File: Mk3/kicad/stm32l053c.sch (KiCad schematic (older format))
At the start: 42 parts, among them J1 GND, J2 GND, J3 TX, J4 GND, J5 TEST_1P, J6 TEST_1P, J7 TEST_1P, J8 RX, P1 SWD, U1 AP2112, U2 STM32L053C8_LQFP48, U3 ADS1015, U4 UFL_SMA, U5 RFM92/95

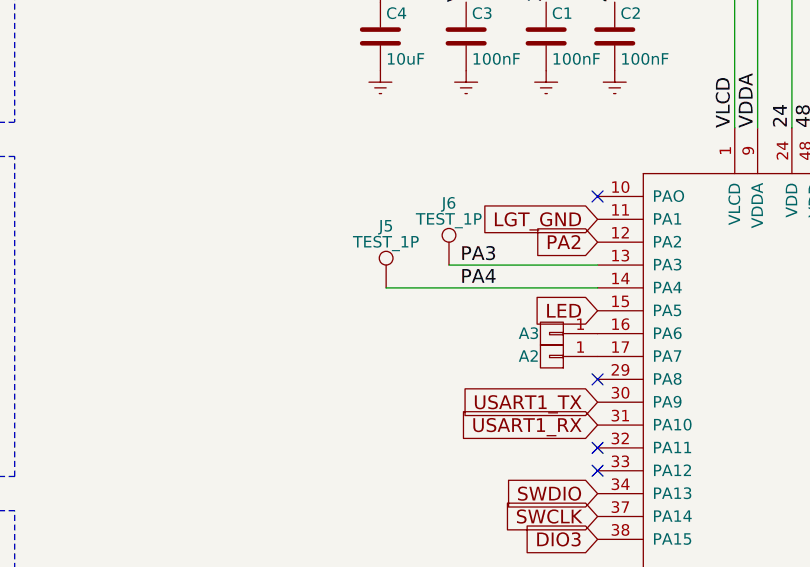
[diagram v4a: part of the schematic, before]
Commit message: Pull up resistor for the DS18B20 one wire temperature sensor
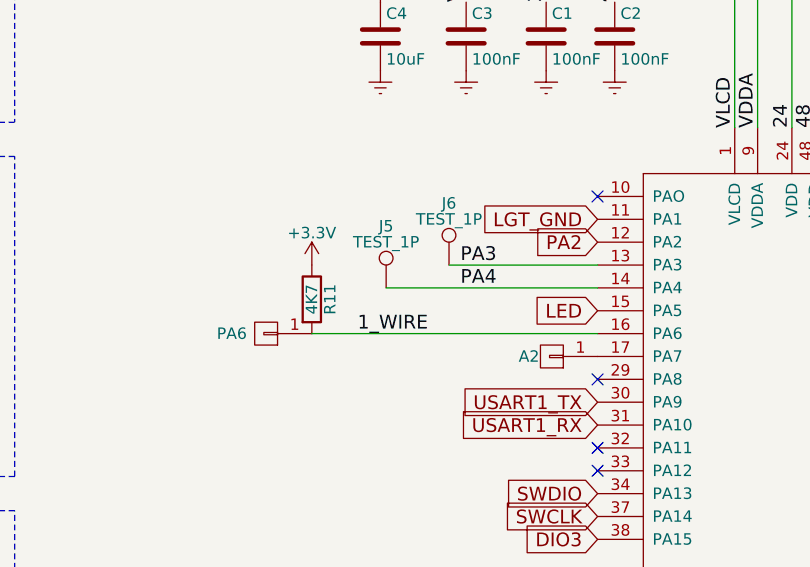
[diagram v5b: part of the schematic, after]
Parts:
- added R11: 4K7, Resistors_SMD:R_0805_HandSoldering, symbol R
- renumbered A3 to PA6
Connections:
- net +3V3: now also R11.1
- net 1_WIRE: now reaches PA6.1 (P1), U2.16 (PA6)
- net 1_WIRE: now also R11.2
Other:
- moved on the sheet: PA6
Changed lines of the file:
@@
 $EndDescr
 $Comp
-L Earth #PWR8
+L Earth #PWR29
 U 1 1 58021BE1
 P 7400 1900
-F 0 "#PWR8" H 7400 1650 50  0001 C CNN
+F 0 "#PWR29" H 7400 1650 50  0001 C CNN
 F 1 "Earth" H 7400 1750 50  0001 C CNN
 F 2 "" H 7400 1900 50  0000 C CNN
@@
 $EndComp
 $Comp
-L GNDA #PWR25
+L GNDA #PWR34
 U 1 1 58021F75
 P 9325 5925
-F 0 "#PWR25" H 9325 5675 50  0001 C CNN
+F 0 "#PWR34" H 9325 5675 50  0001 C CNN
 F 1 "GNDA" H 9325 5775 50  0000 C CNN
 F 2 "" H 9325 5925 50  0000 C CNN
@@
 $EndComp
 $Comp
-L Earth #PWR26
+L Earth #PWR35
 U 1 1 58021F89
 P 9825 5925
-F 0 "#PWR26" H 9825 5675 50  0001 C CNN
+F 0 "#PWR35" H 9825 5675 50  0001 C CNN
 F 1 "Earth" H 9825 5775 50  0001 C CNN
 F 2 "" H 9825 5925 50  0000 C CNN
@@
 $EndComp
 $Comp
-L GNDA #PWR27
+L GNDA #PWR31
 U 1 1 58022154
 P 8175 5950
-F 0 "#PWR27" H 8175 5700 50  0001 C CNN
+F 0 "#PWR31" H 8175 5700 50  0001 C CNN
 F 1 "GNDA" H 8175 5800 50  0000 C CNN
 F 2 "" H 8175 5950 50  0000 C CNN
@@
 $EndComp
 $Comp
-L Earth #PWR28
+L Earth #PWR33
 U 1 1 580221FA
 P 8675 5950
-F 0 "#PWR28" H 8675 5700 50  0001 C CNN
+F 0 "#PWR33" H 8675 5700 50  0001 C CNN
 F 1 "Earth" H 8675 5800 50  0001 C CNN
 F 2 "" H 8675 5950 50  0000 C CNN
@@
 $EndComp
 $Comp
-L Earth #PWR13
+L Earth #PWR7
 U 1 1 580369A9
 P 2425 3075
-F 0 "#PWR13" H 2425 2825 50  0001 C CNN
+F 0 "#PWR7" H 2425 2825 50  0001 C CNN
 F 1 "Earth" H 2425 2925 50  0001 C CNN
 F 2 "" H 2425 3075 50  0000 C CNN
@@
 NRST
 $Comp
-L Earth #PWR6
+L Earth #PWR26
 U 1 1 58039244
 P 6675 1900
-F 0 "#PWR6" H 6675 1650 50  0001 C CNN
+F 0 "#PWR26" H 6675 1650 50  0001 C CNN
 F 1 "Earth" H 6675 1750 50  0001 C CNN
 F 2 "" H 6675 1900 50  0000 C CNN
@@
 $EndComp
 $Comp
-L Earth #PWR7
+L Earth #PWR27
 U 1 1 5803BDC8
 P 7050 1900
-F 0 "#PWR7" H 7050 1650 50  0001 C CNN
+F 0 "#PWR27" H 7050 1650 50  0001 C CNN
 F 1 "Earth" H 7050 1750 50  0001 C CNN
 F 2 "" H 7050 1900 50  0000 C CNN
@@
 $EndComp
 $Comp
-L Earth #PWR21
+L Earth #PWR28
 U 1 1 58065816
 P 7275 4950
-F 0 "#PWR21" H 7275 4700 50  0001 C CNN
+F 0 "#PWR28" H 7275 4700 50  0001 C CNN
 F 1 "Earth" H 7275 4800 50  0001 C CNN
 F 2 "" H 7275 4950 50  0000 C CNN
@@
 $EndComp
 $Comp
-L Earth #PWR11
+L Earth #PWR15
 U 1 1 58077163
 P 3550 2800
-F 0 "#PWR11" H 3550 2550 50  0001 C CNN
+F 0 "#PWR15" H 3550 2550 50  0001 C CNN
 F 1 "Earth" H 3550 2650 50  0001 C CNN
 F 2 "" H 3550 2800 50  0000 C CNN
@@
 Place on Top layer
 $Comp
-L Earth #PWR23
+L Earth #PWR11
 U 1 1 592DF55A
 P 2900 5450
-F 0 "#PWR23" H 2900 5200 50  0001 C CNN
+F 0 "#PWR11" H 2900 5200 50  0001 C CNN
 F 1 "Earth" H 2900 5300 50  0001 C CNN
 F 2 "" H 2900 5450 50  0000 C CNN
@@
 NoConn ~ 4150 1625
 $Comp
-L Earth #PWR10
+L Earth #PWR17
 U 1 1 592F1C89
 P 3750 1925
-F 0 "#PWR10" H 3750 1675 50  0001 C CNN
+F 0 "#PWR17" H 3750 1675 50  0001 C CNN
 F 1 "Earth" H 3750 1775 50  0001 C CNN
 F 2 "" H 3750 1925 50  0000 C CNN
@@
 RFM_RST
 $Comp
-L +3.3V #PWR1
+L +3.3V #PWR21
 U 1 1 592F43A5
 P 4450 1175
-F 0 "#PWR1" H 4450 1025 50  0001 C CNN
+F 0 "#PWR21" H 4450 1025 50  0001 C CNN
 F 1 "+3.3V" H 4450 1315 50  0000 C CNN
 F 2 "" H 4450 1175 50  0001 C CNN
@@
 $EndComp
 $Comp
-L +3.3V #PWR12
+L +3.3V #PWR5
 U 1 1 592F4BC3
 P 1925 2875
-F 0 "#PWR12" H 1925 2725 50  0001 C CNN
+F 0 "#PWR5" H 1925 2725 50  0001 C CNN
 F 1 "+3.3V" H 1925 3015 50  0000 C CNN
 F 2 "" H 1925 2875 50  0001 C CNN
@@
 $EndComp
 $Comp
-L +3.3V #PWR2
+L +3.3V #PWR32
 U 1 1 592F4E66
 P 8475 1425
-F 0 "#PWR2" H 8475 1275 50  0001 C CNN
+F 0 "#PWR32" H 8475 1275 50  0001 C CNN
 F 1 "+3.3V" H 8475 1565 50  0000 C CNN
 F 2 "" H 8475 1425 50  0001 C CNN
@@
 $EndComp
 $Comp
-L +3.3V #PWR32
+L +3.3V #PWR22
 U 1 1 592F53D7
 P 4775 6725
-F 0 "#PWR32" H 4775 6575 50  0001 C CNN
+F 0 "#PWR22" H 4775 6575 50  0001 C CNN
 F 1 "+3.3V" H 4775 6865 50  0000 C CNN
 F 2 "" H 4775 6725 50  0001 C CNN
@@
 $EndComp
 $Comp
-L +3.3V #PWR3
+L +3.3V #PWR25
 U 1 1 592F54CD
 P 6675 1600
-F 0 "#PWR3" H 6675 1450 50  0001 C CNN
+F 0 "#PWR25" H 6675 1450 50  0001 C CNN
 F 1 "+3.3V" H 6675 1740 50  0000 C CNN
 F 2 "" H 6675 1600 50  0001 C CNN
@@
 NoConn ~ 7625 3550
 $Comp
-L Earth #PWR33
+L Earth #PWR23
 U 1 1 592F7C8A
 P 4775 7025
-F 0 "#PWR33" H 4775 6775 50  0001 C CNN
+F 0 "#PWR23" H 4775 6775 50  0001 C CNN
 F 1 "Earth" H 4775 6875 50  0001 C CNN
 F 2 "" H 4775 7025 50  0000 C CNN
@@
 $EndComp
 $Comp
-L Earth #PWR29
+L Earth #PWR9
 U 1 1 592F7CF0
 P 2750 6425
-F 0 "#PWR29" H 2750 6175 50  0001 C CNN
+F 0 "#PWR9" H 2750 6175 50  0001 C CNN
 F 1 "Earth" H 2750 6275 50  0001 C CNN
 F 2 "" H 2750 6425 50  0000 C CNN
@@
 $EndComp
 $Comp
-L Earth #PWR34
+L Earth #PWR12
 U 1 1 592F7EE4
 P 3225 7125
-F 0 "#PWR34" H 3225 6875 50  0001 C CNN
+F 0 "#PWR12" H 3225 6875 50  0001 C CNN
 F 1 "Earth" H 3225 6975 50  0001 C CNN
 F 2 "" H 3225 7125 50  0000 C CNN
@@
 $EndComp
 $Comp
-L Earth #PWR30
+L Earth #PWR2
 U 1 1 592F80DC
 P 1300 6575
-F 0 "#PWR30" H 1300 6325 50  0001 C CNN
+F 0 "#PWR2" H 1300 6325 50  0001 C CNN
 F 1 "Earth" H 1300 6425 50  0001 C CNN
 F 2 "" H 1300 6575 50  0000 C CNN
@@
 $EndComp
 $Comp
-L Earth #PWR31
+L Earth #PWR6
 U 1 1 592F814F
 P 2050 6600
-F 0 "#PWR31" H 2050 6350 50  0001 C CNN
+F 0 "#PWR6" H 2050 6350 50  0001 C CNN
 F 1 "Earth" H 2050 6450 50  0001 C CNN
 F 2 "" H 2050 6600 50  0000 C CNN
@@
 $EndComp
 $Comp
-L Earth #PWR22
+L Earth #PWR18
 U 1 1 59301904
 P 3800 5150
-F 0 "#PWR22" H 3800 4900 50  0001 C CNN
+F 0 "#PWR18" H 3800 4900 50  0001 C CNN
 F 1 "Earth" H 3800 5000 50  0001 C CNN
 F 2 "" H 3800 5150 50  0000 C CNN
@@
 $EndComp
 $Comp
-L Earth #PWR19
+L Earth #PWR16
 U 1 1 593024E3
 P 3700 4450
-F 0 "#PWR19" H 3700 4200 50  0001 C CNN
+F 0 "#PWR16" H 3700 4200 50  0001 C CNN
 F 1 "Earth" H 3700 4300 50  0001 C CNN
 F 2 "" H 3700 4450 50  0000 C CNN
@@
 $EndComp
 $Comp
-L +3.3V #PWR17
+L +3.3V #PWR10
 U 1 1 59303669
 P 2900 4150
-F 0 "#PWR17" H 2900 4000 50  0001 C CNN
+F 0 "#PWR10" H 2900 4000 50  0001 C CNN
 F 1 "+3.3V" H 2900 4290 50  0000 C CNN
 F 2 "" H 2900 4150 50  0001 C CNN
@@
 $EndComp
 $Comp
-L +3.3V #PWR18
+L +3.3V #PWR19
 U 1 1 59303771
 P 4100 4150
-F 0 "#PWR18" H 4100 4000 50  0001 C CNN
+F 0 "#PWR19" H 4100 4000 50  0001 C CNN
 F 1 "+3.3V" H 4100 4290 50  0000 C CNN
 F 2 "" H 4100 4150 50  0001 C CNN
@@
 $EndComp
 $Comp
-L Earth #PWR4
+L Earth #PWR8
 U 1 1 59316863
 P 2600 1675
-F 0 "#PWR4" H 2600 1425 50  0001 C CNN
+F 0 "#PWR8" H 2600 1425 50  0001 C CNN
 F 1 "Earth" H 2600 1525 50  0001 C CNN
 F 2 "" H 2600 1675 50  0000 C CNN
@@
 $EndComp
 $Comp
-L Earth #PWR20
+L Earth #PWR1
 U 1 1 593290F6
 P 1275 4775
-F 0 "#PWR20" H 1275 4525 50  0001 C CNN
+F 0 "#PWR1" H 1275 4525 50  0001 C CNN
 F 1 "Earth" H 1275 4625 50  0001 C CNN
 F 2 "" H 1275 4775 50  0000 C CNN
@@
 $EndComp
 $Comp
-L Earth #PWR5
+L Earth #PWR3
 U 1 1 59355822
 P 1650 1900
-F 0 "#PWR5" H 1650 1650 50  0001 C CNN
+F 0 "#PWR3" H 1650 1650 50  0001 C CNN
 F 1 "Earth" H 1650 1750 50  0001 C CNN
 F 2 "" H 1650 1900 50  0000 C CNN
@@
 $EndComp
 $Comp
-L Earth #PWR24
+L Earth #PWR4
 U 1 1 59357323
 P 1900 5500
-F 0 "#PWR24" H 1900 5250 50  0001 C CNN
+F 0 "#PWR4" H 1900 5250 50  0001 C CNN
 F 1 "Earth" H 1900 5350 50  0001 C CNN
 F 2 "" H 1900 5500 50  0000 C CNN
@@
 $EndComp
 $Comp
-L Earth #PWR9
+L Earth #PWR30
 U 1 1 59375C9C
 P 7700 1900
-F 0 "#PWR9" H 7700 1650 50  0001 C CNN
+F 0 "#PWR30" H 7700 1650 50  0001 C CNN
 F 1 "Earth" H 7700 1750 50  0001 C CNN
 F 2 "" H 7700 1900 50  0000 C CNN
@@
 $EndComp
 $Comp
-L Earth #PWR16
+L Earth #PWR20
 U 1 1 59379ABF
 P 4175 3450
-F 0 "#PWR16" H 4175 3200 50  0001 C CNN
+F 0 "#PWR20" H 4175 3200 50  0001 C CNN
 F 1 "Earth" H 4175 3300 50  0001 C CNN
 F 2 "" H 4175 3450 50  0000 C CNN
@@
 $EndComp
 $Comp
-L CONN_01X01 A3
+L CONN_01X01 PA6
 U 1 1 593959A7
-P 7425 3050
-F 0 "A3" H 7525 3050 50  0000 C CNN
-F 1 "A3" V 7525 3050 50  0001 C CNN
-F 2 "Pin_Headers:Pin_Header_Straight_1x01_Pitch2.54mm" H 7425 3050 50  0001 C CNN
-F 3 "" H 7425 3050 50  0001 C CNN
-	1    7425 3050
+P 6175 3050
+F 0 "PA6" H 6325 3050 50  0000 C CNN
+F 1 "A3" V 6275 3050 50  0001 C CNN
+F 2 "Pin_Headers:Pin_Header_Straight_1x01_Pitch2.54mm" H 6175 3050 50  0001 C CNN
+F 3 "" H 6175 3050 50  0001 C CNN
+	1    6175 3050
 	-1   0    0    1
 $EndComp
@@
 $EndComp
 $Comp
-L Earth #PWR15
+L Earth #PWR14
 U 1 1 593AA95B
 P 3525 3425
-F 0 "#PWR15" H 3525 3175 50  0001 C CNN
+F 0 "#PWR14" H 3525 3175 50  0001 C CNN
 F 1 "Earth" H 3525 3275 50  0001 C CNN
 F 2 "" H 3525 3425 50  0000 C CNN
@@
 $EndComp
 $Comp
-L Earth #PWR14
+L Earth #PWR13
 U 1 1 593AA9D2
 P 3525 3175
-F 0 "#PWR14" H 3525 2925 50  0001 C CNN
+F 0 "#PWR13" H 3525 2925 50  0001 C CNN
 F 1 "Earth" H 3525 3025 50  0001 C CNN
 F 2 "" H 3525 3175 50  0000 C CNN
@@
 Connection ~ 4400 4950
 Connection ~ 4200 4250
+$Comp
+L R R11
+U 1 1 594FB0BF
+P 6375 2900
+F 0 "R11" V 6455 2900 50  0000 C CNN
+F 1 "4K7" V 6375 2900 50  0000 C CNN
+F 2 "Resistors_SMD:R_0805_HandSoldering" V 6305 2900 50  0001 C CNN
+F 3 "" H 6375 2900 50  0000 C CNN
+	1    6375 2900
+	1    0    0    -1
+$EndComp
+$Comp
+L +3.3V #PWR24
+U 1 1 594FB3E7
+P 6375 2750
+F 0 "#PWR24" H 6375 2600 50  0001 C CNN
+F 1 "+3.3V" H 6375 2890 50  0000 C CNN
+F 2 "" H 6375 2750 50  0001 C CNN
+F 3 "" H 6375 2750 50  0001 C CNN
+	1    6375 2750
+	1    0    0    -1
+$EndComp
+Wire Wire Line
+	7625 3050 6375 3050
+Text Label 6575 3050 0    60   ~ 0
+1_WIRE
 $EndSCHEMATC

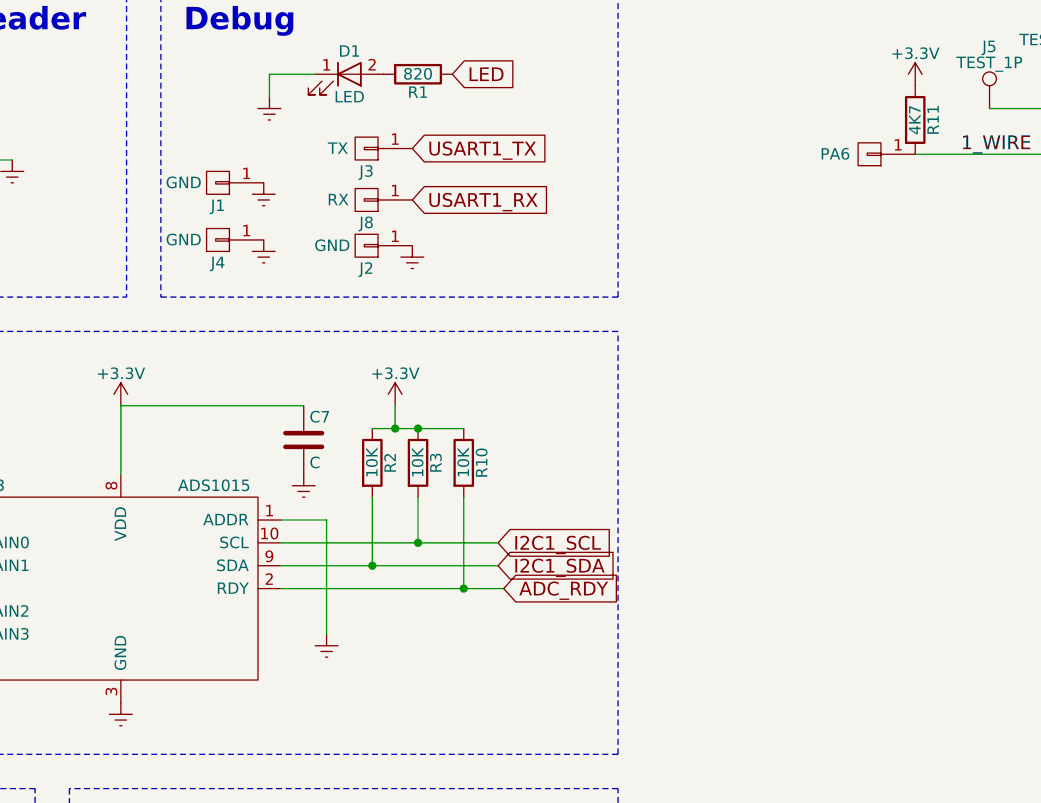
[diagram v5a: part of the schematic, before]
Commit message: Extra 3v3 pins
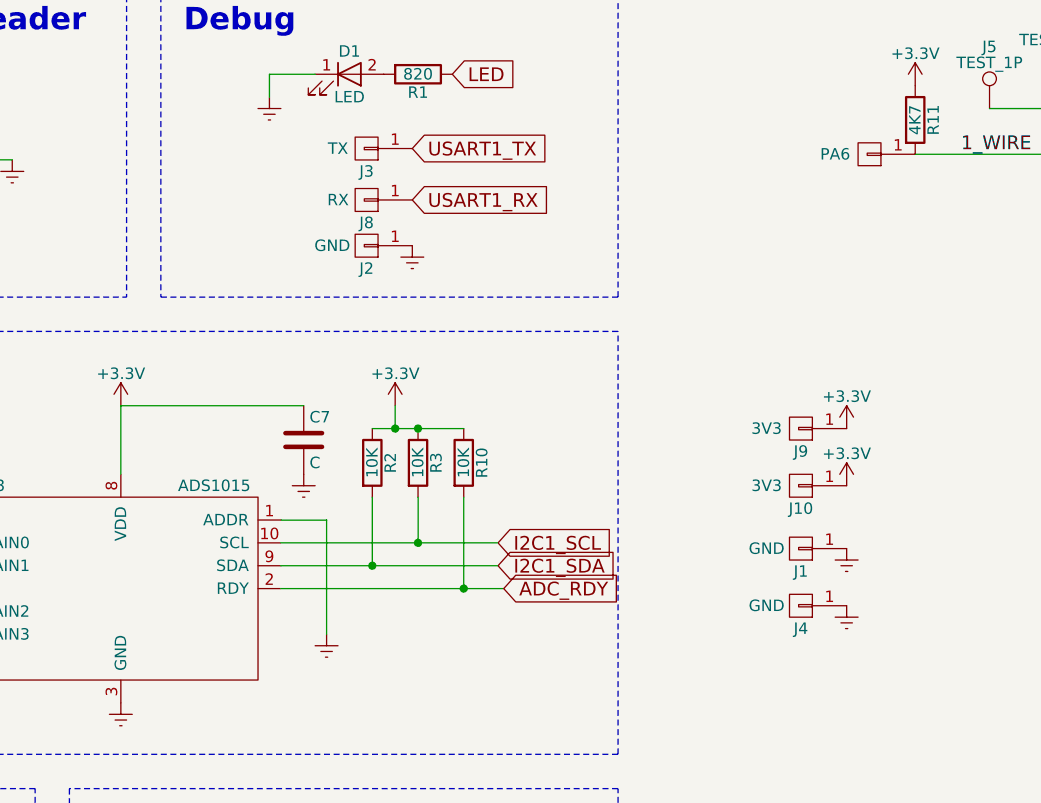
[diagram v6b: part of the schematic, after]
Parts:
- added J10, J9: 3V3, Pin_Headers:Pin_Header_Straight_1x01_Pitch2.54mm, symbol CONN_01X01
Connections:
- net +3V3: now also J10.1 (P1), J9.1 (P1)
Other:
- moved on the sheet: J1, J4

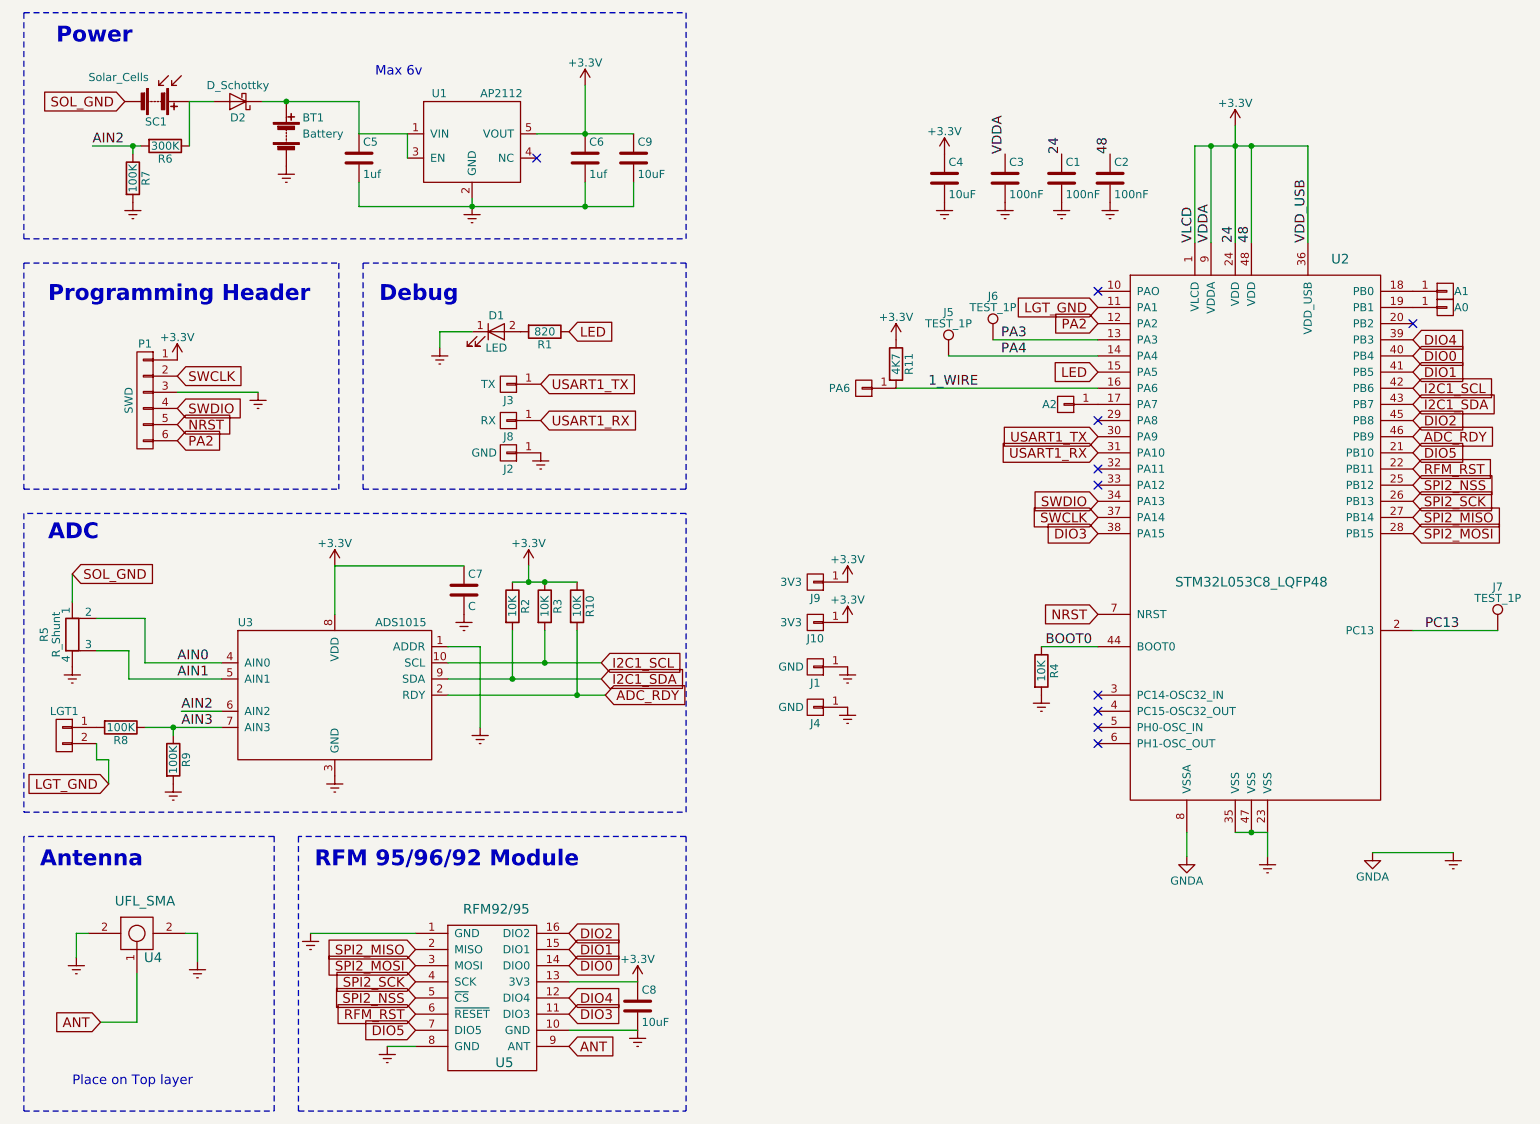
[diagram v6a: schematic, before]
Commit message: Measure battery voltage with the external ADC
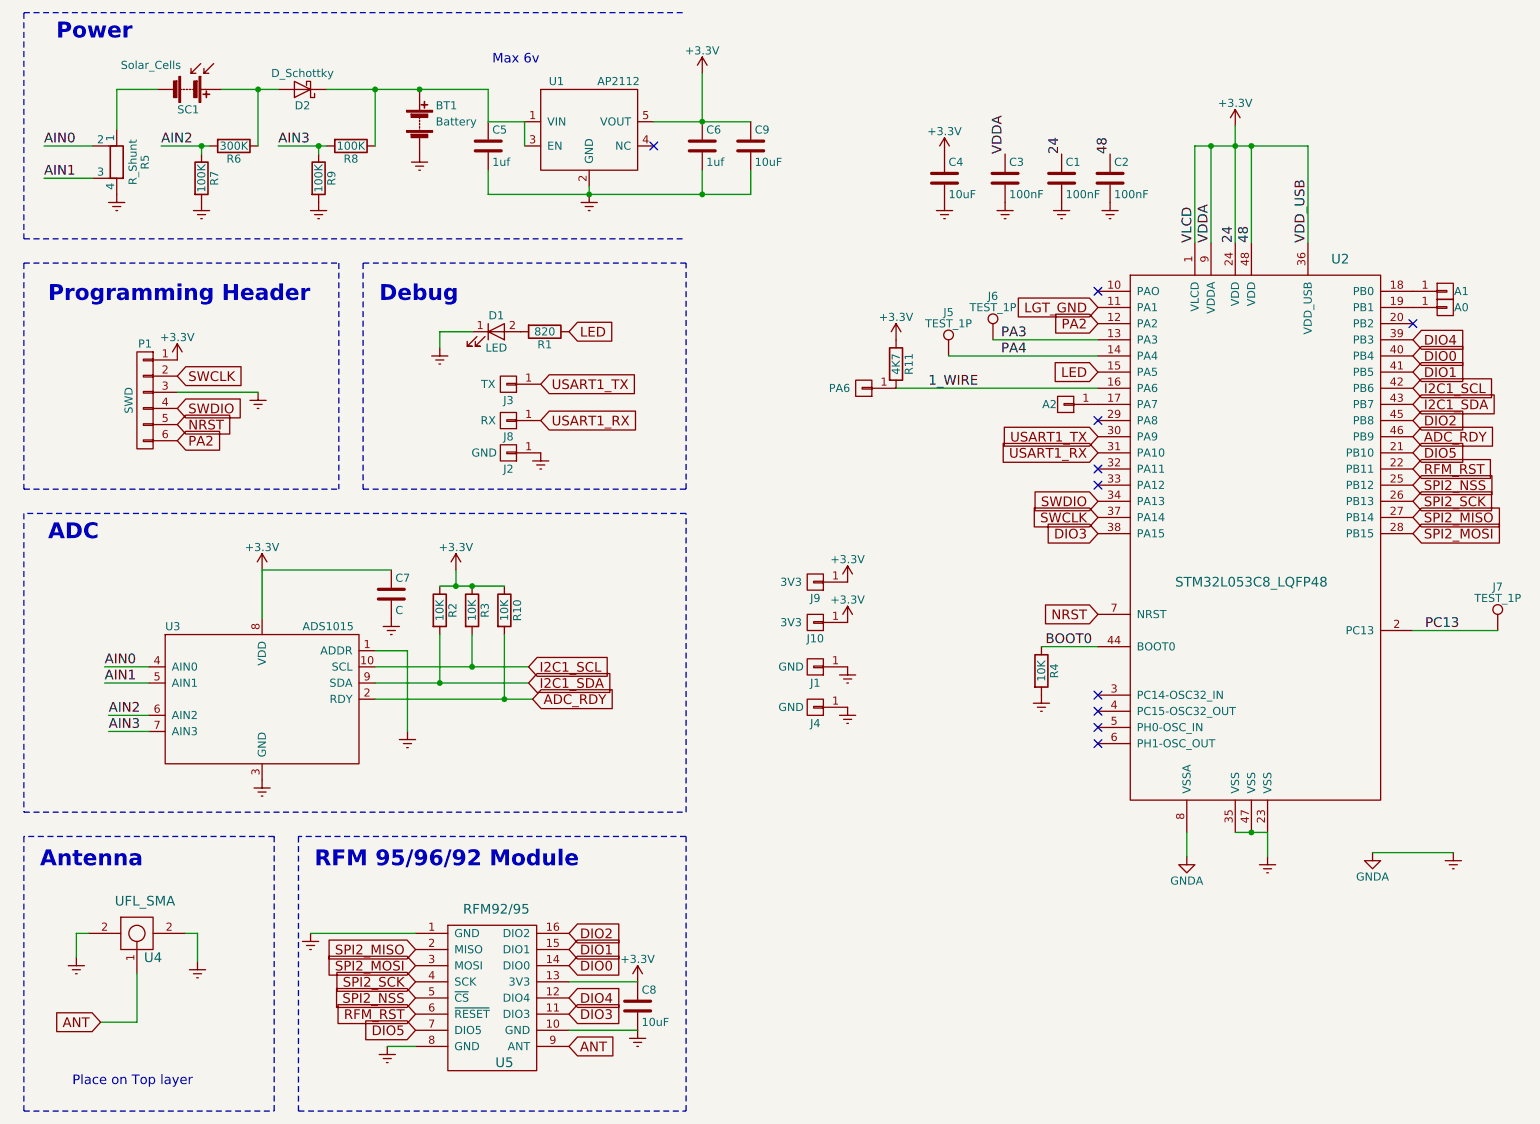
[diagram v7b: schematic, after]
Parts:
- removed LGT1: LGT, Pin_Headers:Pin_Header_Straight_1x02_Pitch2.54mm, symbol CONN_01X02
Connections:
- net AIN3: now also R8.2; no longer R8.1
- net at BT1.1 (+), C5.1, D2.1 (K)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: now also R8.1
- net SOL_GND: no longer names the net of R5.1, SC1.2 (-)
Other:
- moved on the sheet: BT1, C5, C6, C7, C9, D2, R10, R2, R3, R5, R6, R7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
